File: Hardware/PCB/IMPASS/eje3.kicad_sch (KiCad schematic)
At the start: 18 parts, among them Q17 BC847BDW1, Q18 DMP3013SFV, Q19 DMN3008SFG, Q20 DMN3008SFG, Q21 DMP3013SFV, Q22 BC847BDW1, Q23 DMN3008SFG, Q24 DMN3008SFG, Q25 DMP3013SFV, Q26 DMP3013SFV

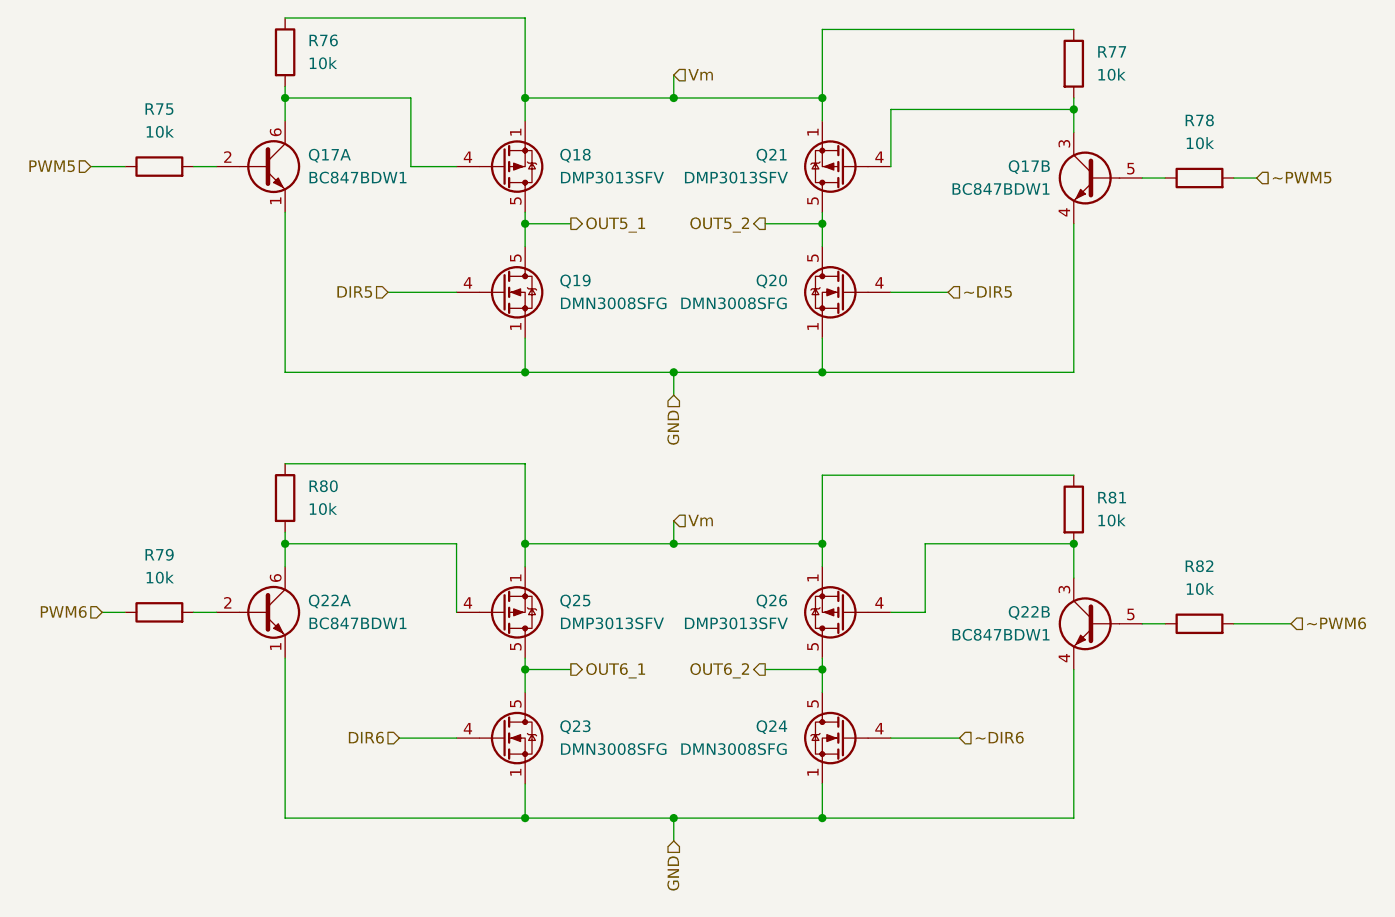
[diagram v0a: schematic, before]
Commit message: Hardware: Update all the logic pcb 	- added ads1015 	- added the logic foe P-MOSFET 	- added I2C connector
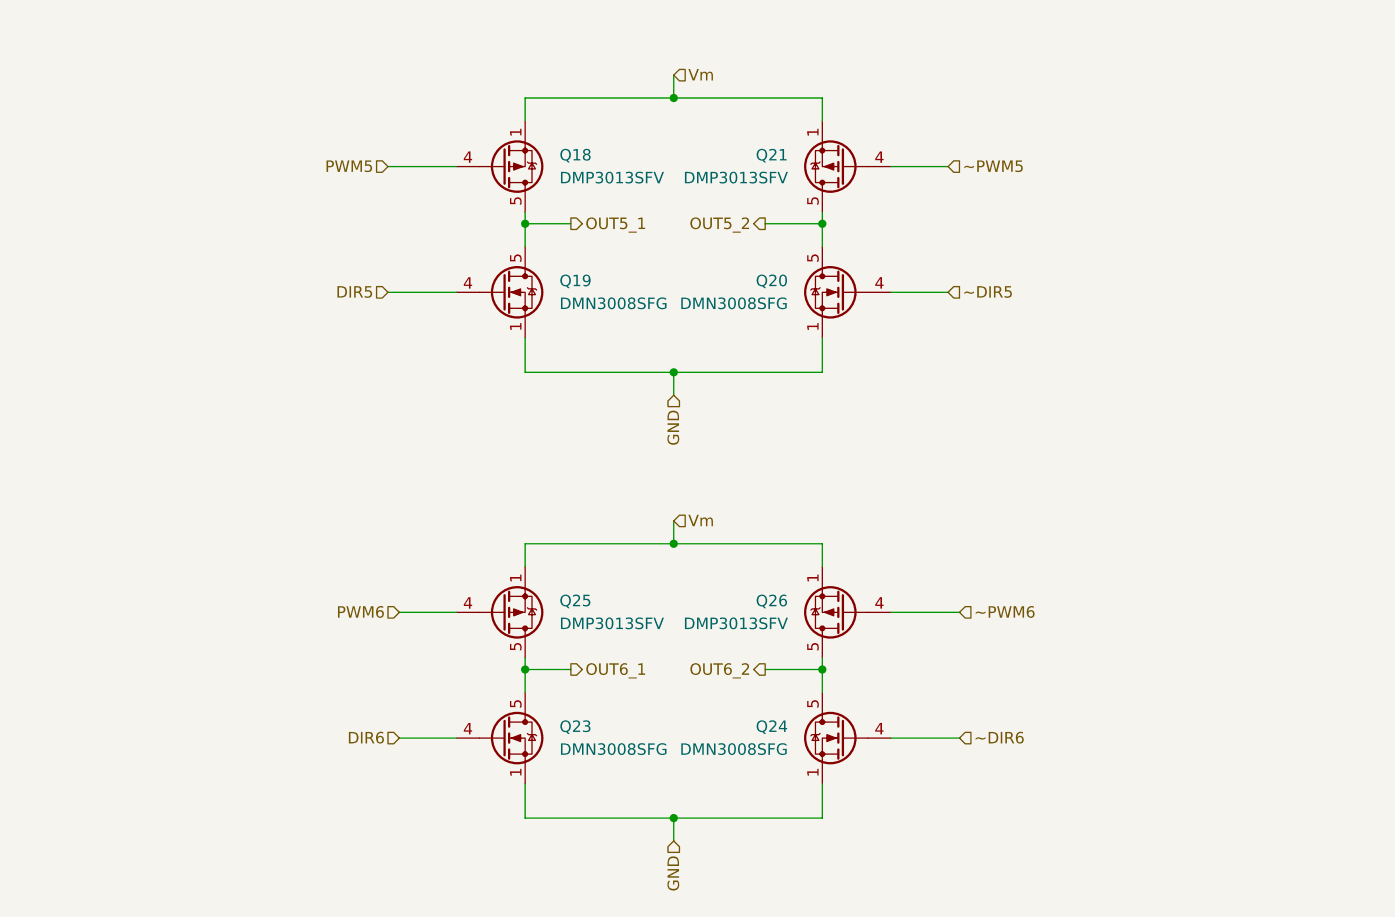
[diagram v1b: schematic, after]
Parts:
- removed Q17, Q22: BC847BDW1, Package_TO_SOT_SMD:SOT-363_SC-70-6, symbol Transistor_BJT:BC847BDW1
- removed R75, R76, R77, R78, R79, R80, R81, R82: 10k, Resistor_SMD:R_0603_1608Metric, symbol Device:R
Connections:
- net PWM5: now also Q18.4 (G)
- net PWM6: now also Q25.4 (G)
- net ~PWM5: now also Q21.4 (G)
- net ~PWM6: now also Q26.4 (G)
